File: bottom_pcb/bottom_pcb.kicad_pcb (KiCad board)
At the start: 2 copper layers, 50 x 50 mm, 14 parts, among them J1 Conn_01x13, J2 Conn_01x13, J3 flat_cable_connector, J4 socket

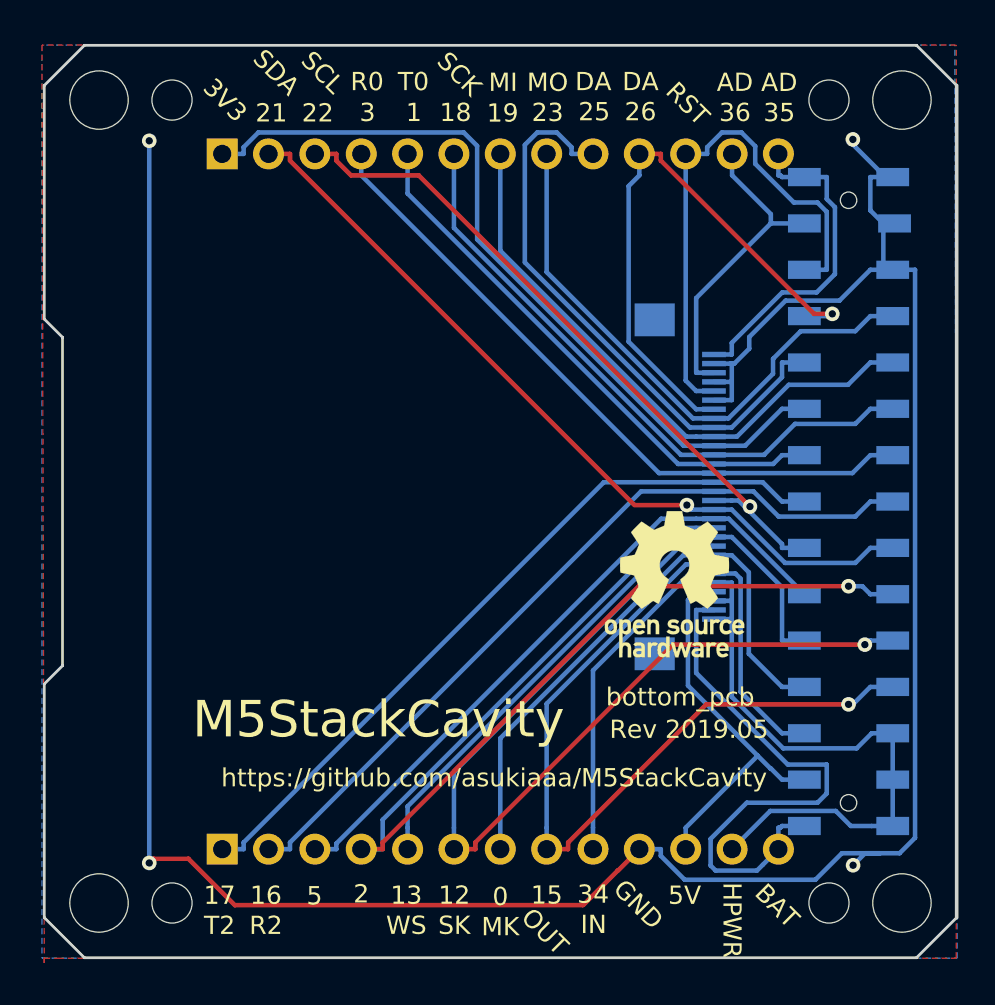
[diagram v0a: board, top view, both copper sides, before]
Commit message: Update center connector position on bottom_pcb
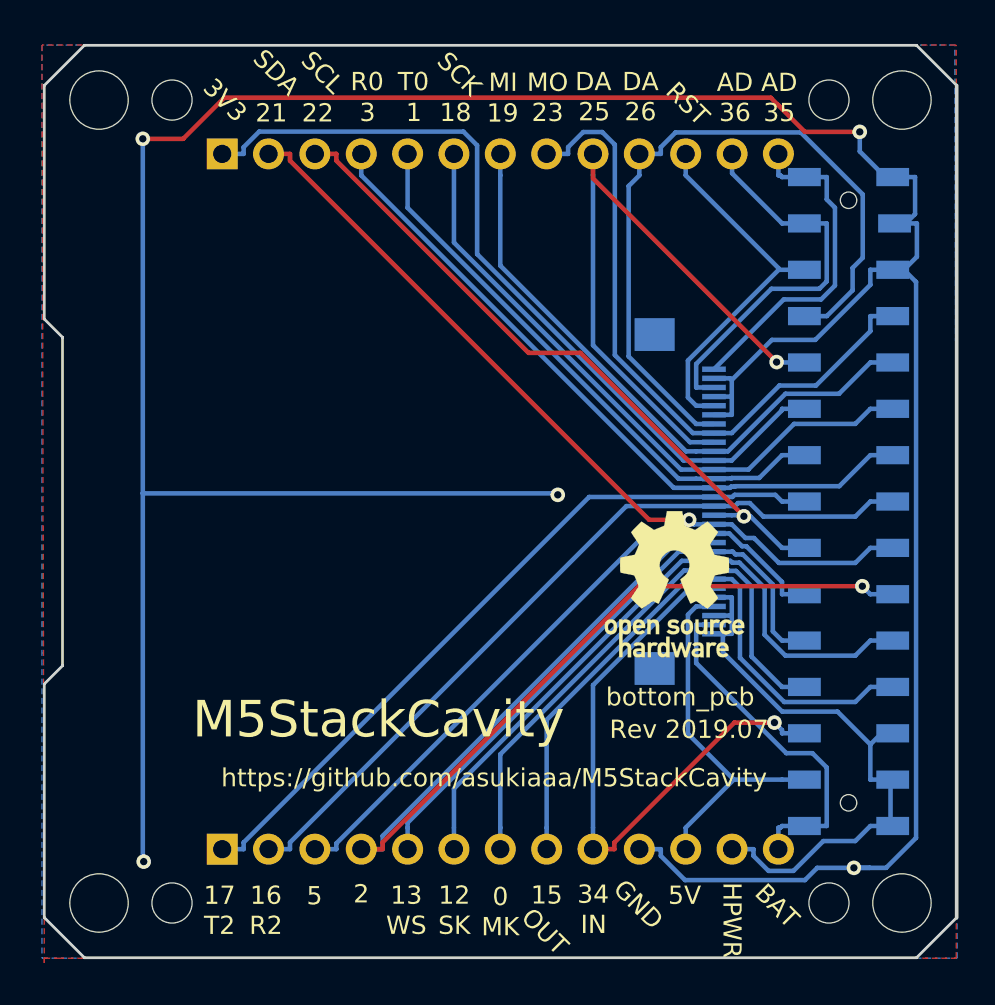
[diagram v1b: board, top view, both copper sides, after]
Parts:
- moved OSHWREF1 16.8 mm to (106.5, 62.0)
- moved J3 0.81 mm to (134.8, 75.0)
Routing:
- net GND: track 146.6 -> 181.5 mm, vias 4 -> 5
- net G12: track 52.6 -> 36.5 mm, vias 1 -> 0
- net +BATT: track 31.0 -> 19.7 mm
- net RST: track 29.4 -> 20.5 mm
- net G15: track 43.2 -> 34.6 mm, vias 1 -> 0
- net G25: track 32.7 -> 40.6 mm, vias 1 -> 0
- net G23: track 31.6 -> 36.4 mm
- net G36: track 17.4 -> 21.9 mm
- net G26: track 32.2 -> 36.4 mm, vias 0 -> 1
- net G34: track 30.8 -> 32.8 mm, vias 0 -> 1
- net G0: track 32.5 -> 31.0 mm
- net G13: track 34.3 -> 32.9 mm
- net G1: track 30.3 -> 31.6 mm
- net +3V3: track 43.6 -> 44.8 mm
- net G19: track 32.7 -> 33.9 mm
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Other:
- board text added: "Rev 2019.07"
- board text removed: "Rev 2019.05"

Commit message: Add center hole to bottom_pcb
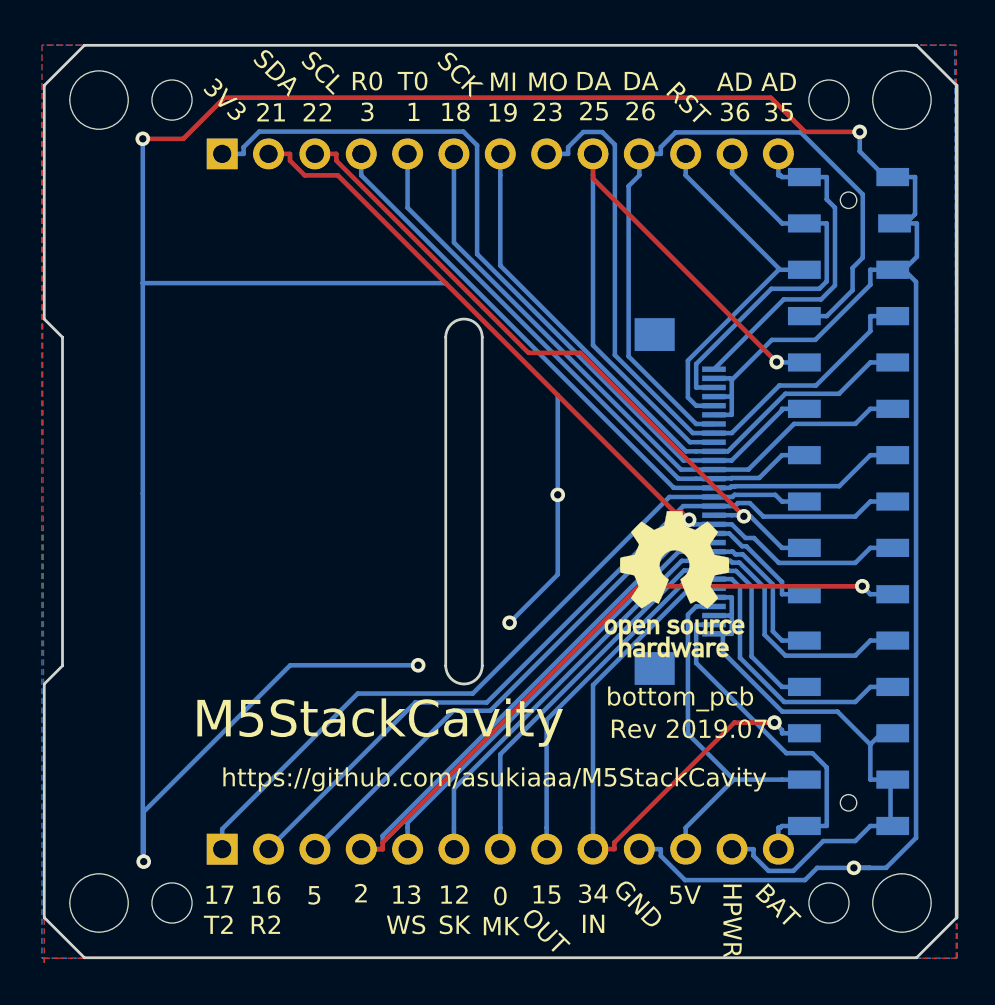
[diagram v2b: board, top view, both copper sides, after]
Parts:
- added REF**: center_hole, footprints:center_hole, F.Cu at (123.0, 75.0)
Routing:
- net GND: track 181.5 -> 218.8 mm, vias 5 -> 7
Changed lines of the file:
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@@
     (thickness 1.6)
     (drawings 64)
-    (tracks 349)
+    (tracks 363)
     (zones 0)
-    (modules 14)
+    (modules 15)
     (nets 27)
   )
@@
     (add_net HPWR)
     (add_net RST)
+  )
+  (module footprints:center_hole (layer F.Cu)
+    (at 123 75)
+    (fp_text reference REF** (at -0.0508 10.922) (layer Edge.Cuts) hide
+      (effects (font (size 1 1) (thickness 0.15)))
+    )
+    (fp_text value center_hole (at 0.127 -10.6934) (layer F.Fab) hide
+      (effects (font (size 1 1) (thickness 0.15)))
+    )
+    (fp_line (start -1 -9) (end -1 9) (layer Edge.Cuts) (width 0.15))
+    (fp_line (start 1 9) (end 1 -9) (layer Edge.Cuts) (width 0.15))
+    (fp_arc (start 0 9) (end -1 9) (angle -180) (layer Edge.Cuts) (width 0.15))
+    (fp_arc (start 0 -9) (end 1 -9) (angle -180) (layer Edge.Cuts) (width 0.15))
   )
   (module footprints:PinSocket_2x15_P2.54mm_Vertical_SMD_just_for_M5Stack_bottom_pcb (layer B.Cu)
@@
   (segment (start 128.0588 74.5532) (end 128.1388 74.6332) (width 0.25) (layer B.Cu) (net 1))
   (via (at 128.1388 74.6332) (size 0.8) (drill 0.4) (layers F.Cu B.Cu) (net 1))
-  (segment (start 105.3988 74.5532) (end 128.0588 74.5532) (width 0.25) (layer B.Cu) (net 1))
   (segment (start 105.3988 74.5532) (end 105.3988 94.6832) (width 0.25) (layer B.Cu) (net 1))
-  (segment (start 105.3988 55.1232) (end 105.3988 74.5532) (width 0.25) (layer B.Cu) (net 1))
+  (segment (start 121.9957 63.0332) (end 105.3988 63.0332) (width 0.25) (layer B.Cu) (net 1))
+  (segment (start 128.1388 69.1763) (end 121.9957 63.0332) (width 0.25) (layer B.Cu) (net 1))
+  (segment (start 128.1388 74.6332) (end 128.1388 69.1763) (width 0.25) (layer B.Cu) (net 1))
+  (segment (start 105.3988 55.1232) (end 105.3988 63.0332) (width 0.25) (layer B.Cu) (net 1))
+  (segment (start 105.3988 63.0332) (end 105.3988 74.5532) (width 0.25) (layer B.Cu) (net 1))
+  (via (at 125.4988 81.6432) (size 0.8) (drill 0.4) (layers F.Cu B.Cu) (net 1))
+  (segment (start 128.1388 74.6332) (end 128.1388 79.0032) (width 0.25) (layer B.Cu) (net 1))
+  (segment (start 128.1388 79.0032) (end 125.4988 81.6432) (width 0.25) (layer B.Cu) (net 1))
+  (segment (start 105.4488 94.7332) (end 105.4488 92.0032) (width 0.25) (layer B.Cu) (net 1))
+  (via (at 120.4888 83.9732) (size 0.8) (drill 0.4) (layers F.Cu B.Cu) (net 1))
+  (segment (start 105.4488 92.0032) (end 113.4788 83.9732) (width 0.25) (layer B.Cu) (net 1))
+  (segment (start 113.4788 83.9732) (end 120.4888 83.9732) (width 0.25) (layer B.Cu) (net 1))
   (segment (start 145.2687 64.84) (end 145.2687 65.6653) (width 0.25) (layer B.Cu) (net 2))
   (segment (start 145.2687 65.6653) (end 142.2896 68.6444) (width 0.25) (layer B.Cu) (net 2))
@@
   (segment (start 134.4947 74.25) (end 136.699 74.25) (width 0.25) (layer B.Cu) (net 5))
   (segment (start 146.494 72.46) (end 145.2687 72.46) (width 0.25) (layer B.Cu) (net 5))
-  (segment (start 112.29 94.05) (end 113.4653 94.05) (width 0.25) (layer B.Cu) (net 6))
-  (segment (start 136.699 75.25) (end 131.898 75.25) (width 0.25) (layer B.Cu) (net 6))
-  (segment (start 131.898 75.25) (end 113.4653 93.6827) (width 0.25) (layer B.Cu) (net 6))
-  (segment (start 113.4653 93.6827) (end 113.4653 94.05) (width 0.25) (layer B.Cu) (net 6))
   (segment (start 145.2687 75) (end 144.4434 75.8253) (width 0.25) (layer B.Cu) (net 6))
   (segment (start 144.4434 75.8253) (end 139.4031 75.8253) (width 0.25) (layer B.Cu) (net 6))
@@
   (segment (start 137.8477 75.25) (end 136.699 75.25) (width 0.25) (layer B.Cu) (net 6))
   (segment (start 146.494 75) (end 145.2687 75) (width 0.25) (layer B.Cu) (net 6))
+  (segment (start 135.015698 75.25) (end 124.252498 86.0132) (width 0.25) (layer B.Cu) (net 6))
+  (segment (start 136.699 75.25) (end 135.015698 75.25) (width 0.25) (layer B.Cu) (net 6))
+  (segment (start 120.3268 86.0132) (end 112.29 94.05) (width 0.25) (layer B.Cu) (net 6))
+  (segment (start 124.252498 86.0132) (end 120.3268 86.0132) (width 0.25) (layer B.Cu) (net 6))
   (segment (start 145.2687 77.54) (end 144.4434 78.3653) (width 0.25) (layer B.Cu) (net 7))
   (segment (start 144.4434 78.3653) (end 140.2589 78.3653) (width 0.25) (layer B.Cu) (net 7))
@@
   (segment (start 138.8921 76.9985) (end 138.4228 76.9985) (width 0.25) (layer B.Cu) (net 7))
   (segment (start 138.4228 76.9985) (end 137.6743 76.25) (width 0.25) (layer B.Cu) (net 7))
-  (segment (start 135.3387 76) (end 133.148 76) (width 0.25) (layer F.Cu) (net 7))
-  (segment (start 133.148 76) (end 113.4653 56.3173) (width 0.25) (layer F.Cu) (net 7))
   (segment (start 113.4653 56.3173) (end 113.4653 55.95) (width 0.25) (layer F.Cu) (net 7))
   (segment (start 136.699 76.25) (end 137.6743 76.25) (width 0.25) (layer B.Cu) (net 7))
@@
   (segment (start 146.494 77.54) (end 145.2687 77.54) (width 0.25) (layer B.Cu) (net 7))
   (via (at 135.3387 76) (size 0.8) (layers F.Cu B.Cu) (net 7))
+  (segment (start 114.273001 57.125001) (end 113.4653 56.3173) (width 0.25) (layer F.Cu) (net 7))
+  (segment (start 134.562501 75.600001) (end 116.087501 57.125001) (width 0.25) (layer F.Cu) (net 7))
+  (segment (start 116.087501 57.125001) (end 114.273001 57.125001) (width 0.25) (layer F.Cu) (net 7))
+  (segment (start 134.938701 75.600001) (end 134.562501 75.600001) (width 0.25) (layer F.Cu) (net 7))
+  (segment (start 135.3387 76) (end 134.938701 75.600001) (width 0.25) (layer F.Cu) (net 7))
   (segment (start 118.5453 94.05) (end 118.5453 93.6827) (width 0.25) (layer F.Cu) (net 8))
   (segment (start 118.5453 93.6827) (end 132.5869 79.6411) (width 0.25) (layer F.Cu) (net 8))
@@
   (segment (start 136.2114 77.75) (end 135.7237 77.75) (width 0.25) (layer B.Cu) (net 16))
   (segment (start 119.91 94.05) (end 119.91 92.8747) (width 0.25) (layer B.Cu) (net 16))
-  (segment (start 116.0053 94.05) (end 116.0053 93.7346) (width 0.25) (layer B.Cu) (net 17))
-  (segment (start 116.0053 93.7346) (end 132.9899 76.75) (width 0.25) (layer B.Cu) (net 17))
-  (segment (start 132.9899 76.75) (end 135.7237 76.75) (width 0.25) (layer B.Cu) (net 17))
   (segment (start 140.4287 80.08) (end 140.4287 79.4067) (width 0.25) (layer B.Cu) (net 17))
   (segment (start 140.4287 79.4067) (end 138.4708 77.4488) (width 0.25) (layer B.Cu) (net 17))
@@
   (segment (start 137.5373 76.75) (end 136.699 76.75) (width 0.25) (layer B.Cu) (net 17))
   (segment (start 141.654 80.08) (end 140.4287 80.08) (width 0.25) (layer B.Cu) (net 17))
-  (segment (start 136.2114 76.75) (end 136.699 76.75) (width 0.25) (layer B.Cu) (net 17))
-  (segment (start 136.2114 76.75) (end 135.7237 76.75) (width 0.25) (layer B.Cu) (net 17))
-  (segment (start 114.83 94.05) (end 116.0053 94.05) (width 0.25) (layer B.Cu) (net 17))
+  (segment (start 134.127109 76.774999) (end 124.438898 86.46321) (width 0.25) (layer B.Cu) (net 17))
+  (segment (start 136.697001 76.774999) (end 134.127109 76.774999) (width 0.25) (layer B.Cu) (net 17))
+  (segment (start 136.699 76.75) (end 136.699 76.773) (width 0.25) (layer B.Cu) (net 17))
+  (segment (start 136.699 76.773) (end 136.697001 76.774999) (width 0.25) (layer B.Cu) (net 17))
+  (segment (start 122.41679 86.46321) (end 114.83 94.05) (width 0.25) (layer B.Cu) (net 17))
+  (segment (start 124.438898 86.46321) (end 122.41679 86.46321) (width 0.25) (layer B.Cu) (net 17))
   (segment (start 141.654 77.54) (end 140.4287 77.54) (width 0.25) (layer B.Cu) (net 18))
   (segment (start 140.4287 77.54) (end 138.6977 75.809) (width 0.25) (layer B.Cu) (net 18))
@@
   (segment (start 137.8275 74.6333) (end 140.062 74.6333) (width 0.25) (layer B.Cu) (net 19))
   (segment (start 140.062 74.6333) (end 140.4287 75) (width 0.25) (layer B.Cu) (net 19))
-  (segment (start 109.75 94.05) (end 110.9253 94.05) (width 0.25) (layer B.Cu) (net 19))
-  (segment (start 110.9253 94.05) (end 110.9253 93.6827) (width 0.25) (layer B.Cu) (net 19))
-  (segment (start 110.9253 93.6827) (end 129.858 74.75) (width 0.25) (layer B.Cu) (net 19))
-  (segment (start 129.858 74.75) (end 136.699 74.75) (width 0.25) (layer B.Cu) (net 19))
   (segment (start 141.654 75) (end 140.4287 75) (width 0.25) (layer B.Cu) (net 19))
+  (segment (start 134.257521 74.75) (end 123.484321 85.5232) (width 0.25) (layer B.Cu) (net 19))
+  (segment (start 136.699 74.75) (end 134.257521 74.75) (width 0.25) (layer B.Cu) (net 19))
+  (segment (start 109.75 92.95) (end 109.75 94.05) (width 0.25) (layer B.Cu) (net 19))
+  (segment (start 117.1768 85.5232) (end 109.75 92.95) (width 0.25) (layer B.Cu) (net 19))
+  (segment (start 123.484321 85.5232) (end 117.1768 85.5232) (width 0.25) (layer B.Cu) (net 19))
   (segment (start 119.91 55.95) (end 119.91 58.9041) (width 0.25) (layer B.Cu) (net 20))
   (segment (start 119.91 58.9041) (end 134.7559 73.75) (width 0.25) (layer B.Cu) (net 20))

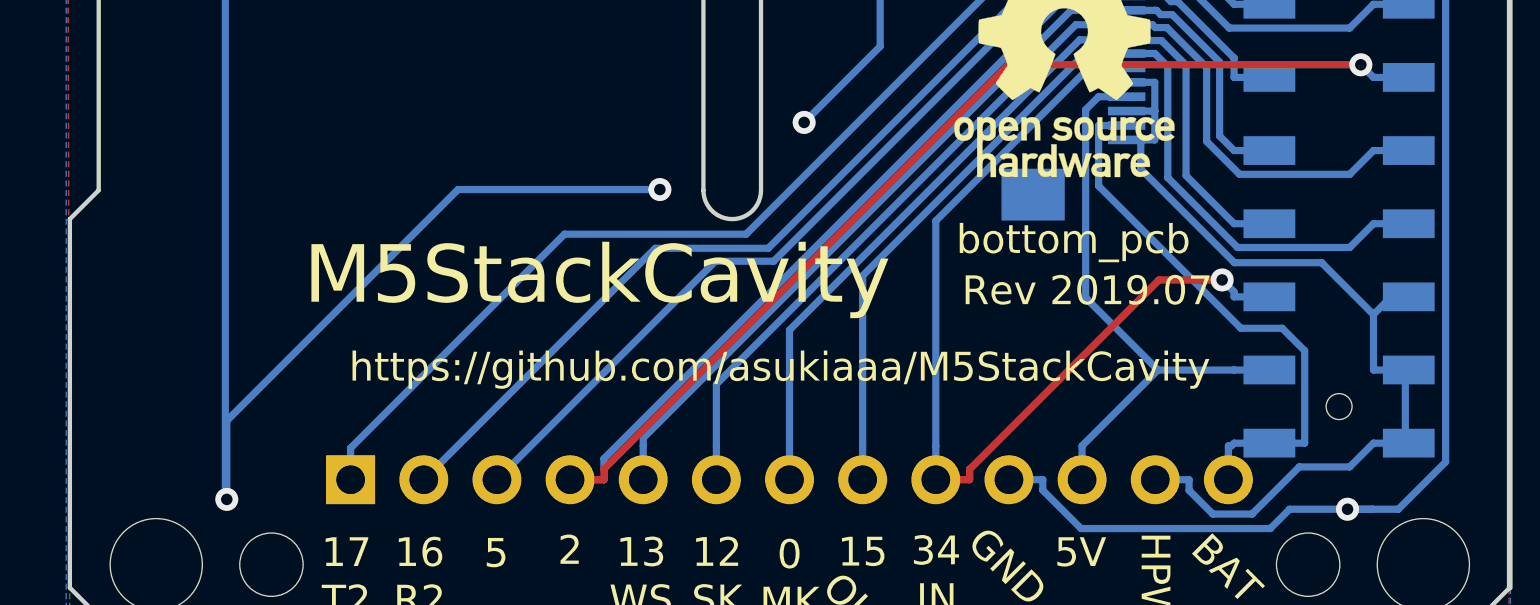
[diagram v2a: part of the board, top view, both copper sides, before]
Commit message: Rename project name to CavityForM5Stack from M5StackCavity
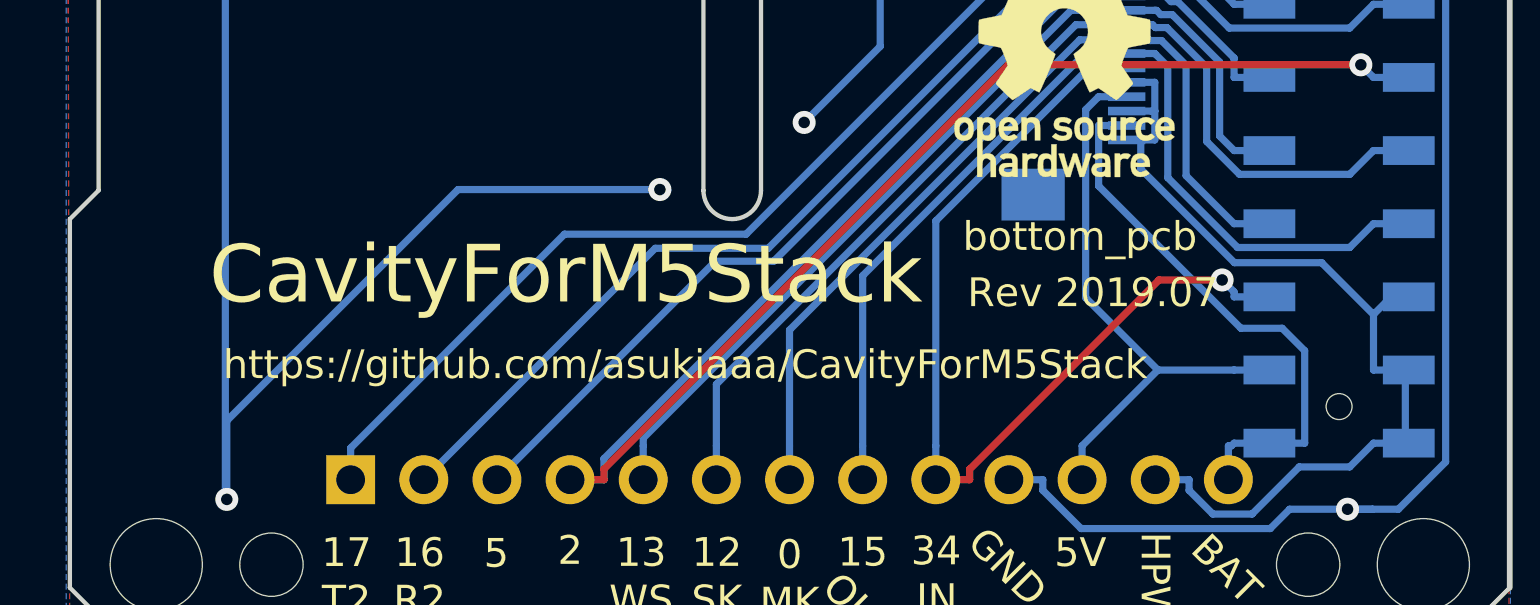
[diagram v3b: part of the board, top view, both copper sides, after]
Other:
- board text added: "CavityForM5Stack"
- board text added: "https://github.com/asukiaaa/CavityForM5Stack"
- board text removed: "M5StackCavity"
- board text removed: "https://github.com/asukiaaa/M5StackCavity"
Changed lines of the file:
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@@
-(kicad_pcb (version 20171130) (host pcbnew 5.1.2-f72e74a~84~ubuntu18.04.1)
+(kicad_pcb (version 20171130) (host pcbnew 5.1.4-e60b266~84~ubuntu18.04.1)
   (general
     (thickness 1.6)
@@
   (gr_line (start 101 66) (end 101 84) (layer Edge.Cuts) (width 0.15))
   (gr_line (start 100 65) (end 101 66) (layer Edge.Cuts) (width 0.15))
-  (gr_text bottom_pcb (at 108.2548 85.4583) (layer B.SilkS)
+  (gr_text bottom_pcb (at 134.4988 89.7832) (layer B.SilkS)
     (effects (font (size 1.2 1.2) (thickness 0.3)) (justify mirror))
   )
-  (gr_text bottom_pcb (at 134.8486 85.7123) (layer F.SilkS)
+  (gr_text bottom_pcb (at 135.0738 85.6082) (layer F.SilkS)
     (effects (font (size 1 1) (thickness 0.25)))
   )
@@
     (effects (font (size 1 1) (thickness 0.25)))
   )
-  (gr_text "Rev 2019.07" (at 135.3312 87.4903) (layer F.SilkS)
-    (effects (font (size 1 1) (thickness 0.25)))
-  )
-  (gr_text M5StackCavity (at 118.3132 86.9442) (layer F.SilkS)
+  (gr_text "Rev 2019.07" (at 135.5238 87.5582) (layer F.SilkS)
+    (effects (font (size 1 1) (thickness 0.25)))
+  )
+  (gr_text CavityForM5Stack (at 117.2238 86.9332) (layer F.SilkS)
     (effects (font (size 2 2) (thickness 0.5)))
   )
-  (gr_text https://github.com/asukiaaa/M5StackCavity (at 121.0437 90.4875) (layer B.SilkS)
-    (effects (font (size 1 1.1) (thickness 0.25)) (justify mirror))
-  )
-  (gr_text https://github.com/asukiaaa/M5StackCavity (at 124.6505 90.1446) (layer F.SilkS)
+  (gr_text https://github.com/asukiaaa/CavityForM5Stack (at 121.3238 91.7082) (layer B.SilkS)
+    (effects (font (size 1 1) (thickness 0.25)) (justify mirror))
+  )
+  (gr_text https://github.com/asukiaaa/CavityForM5Stack (at 121.3738 90.0582) (layer F.SilkS)
     (effects (font (size 1 1) (thickness 0.25)))
   )
@@
     (effects (font (size 1 1) (thickness 0.25)))
   )
-  (gr_text "Rev 2019.07" (at 107.5055 87.63) (layer B.SilkS)
+  (gr_text "Rev 2019.07" (at 122.9238 89.8832) (layer B.SilkS)
     (effects (font (size 1.2 1.2) (thickness 0.3)) (justify mirror))
   )
-  (gr_text M5StackCavity (at 127.0762 86.9188) (layer B.SilkS)
+  (gr_text CavityForM5Stack (at 124.2488 86.9832) (layer B.SilkS)
     (effects (font (size 2.4 2.4) (thickness 0.6)) (justify mirror))
   )
